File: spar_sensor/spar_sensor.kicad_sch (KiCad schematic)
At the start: 24 parts, among them J1 Conn_01x03_Pin, J2 Conn_01x04_Pin, J3 Conn_01x04_Pin, J4 AVR-ISP-6, Q1 MMS8550, Q2 2N7002K, SW1 SW_DPST_x2, U1 HX711, U2 ATtiny85-20M

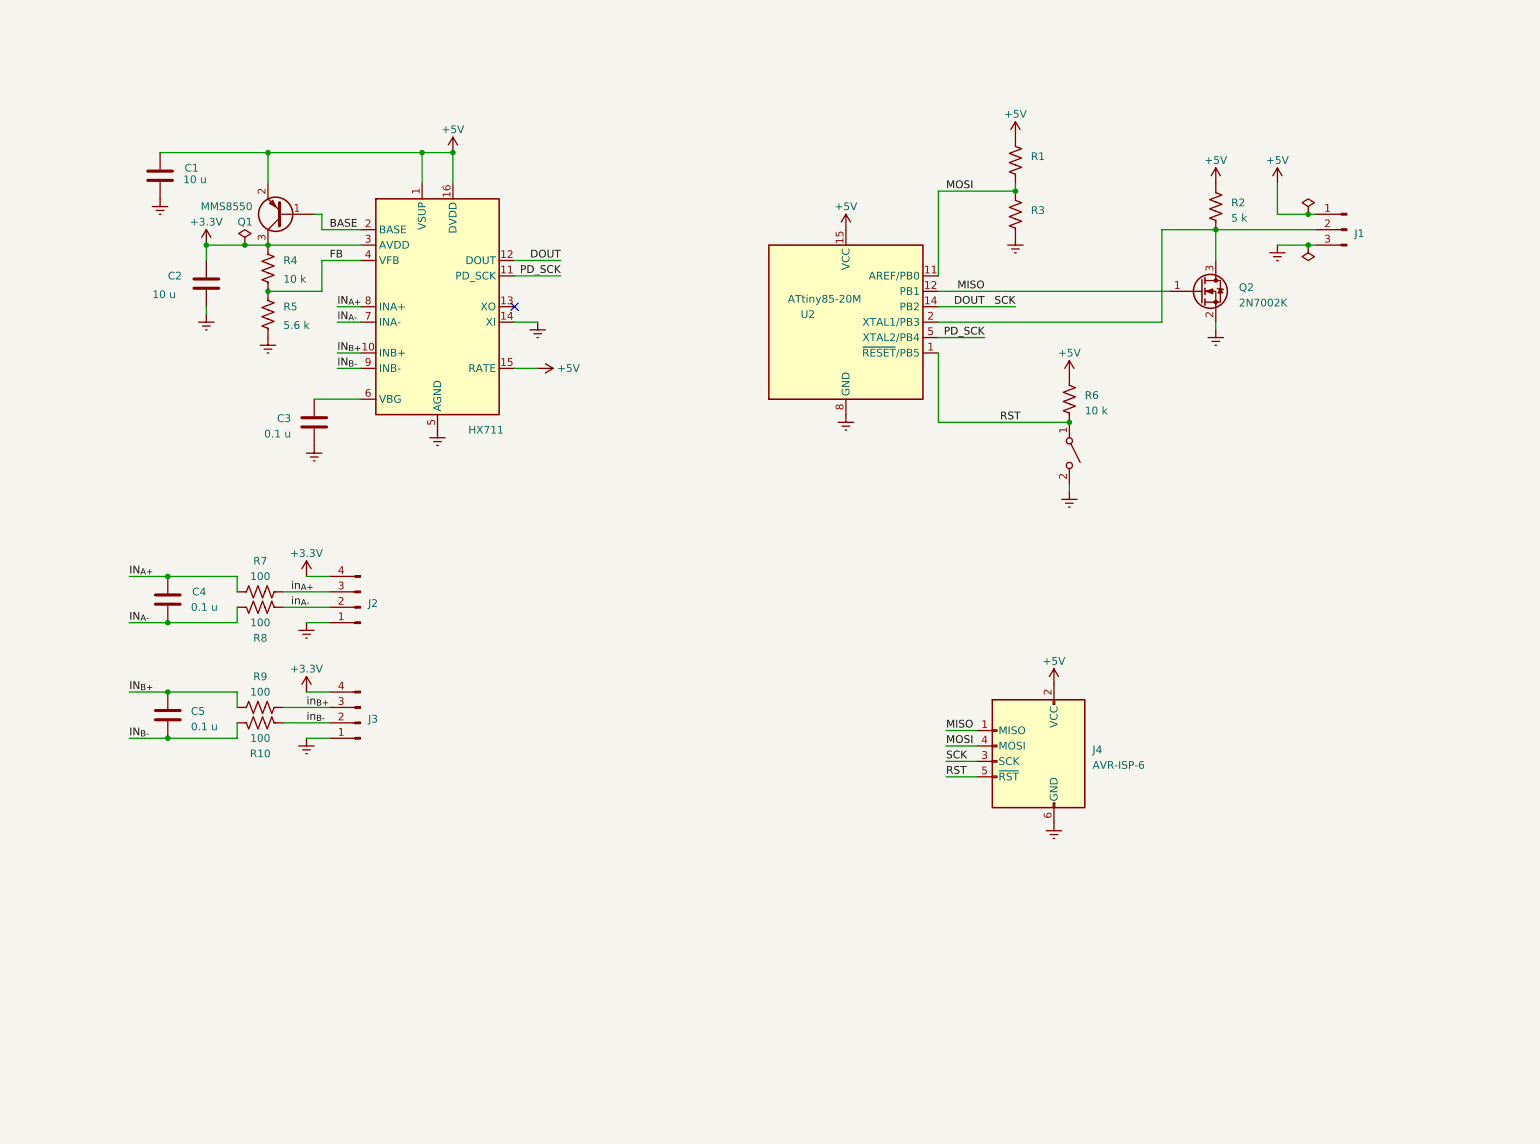
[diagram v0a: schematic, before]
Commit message: Touched up spar sensor to reflect parts as ordered
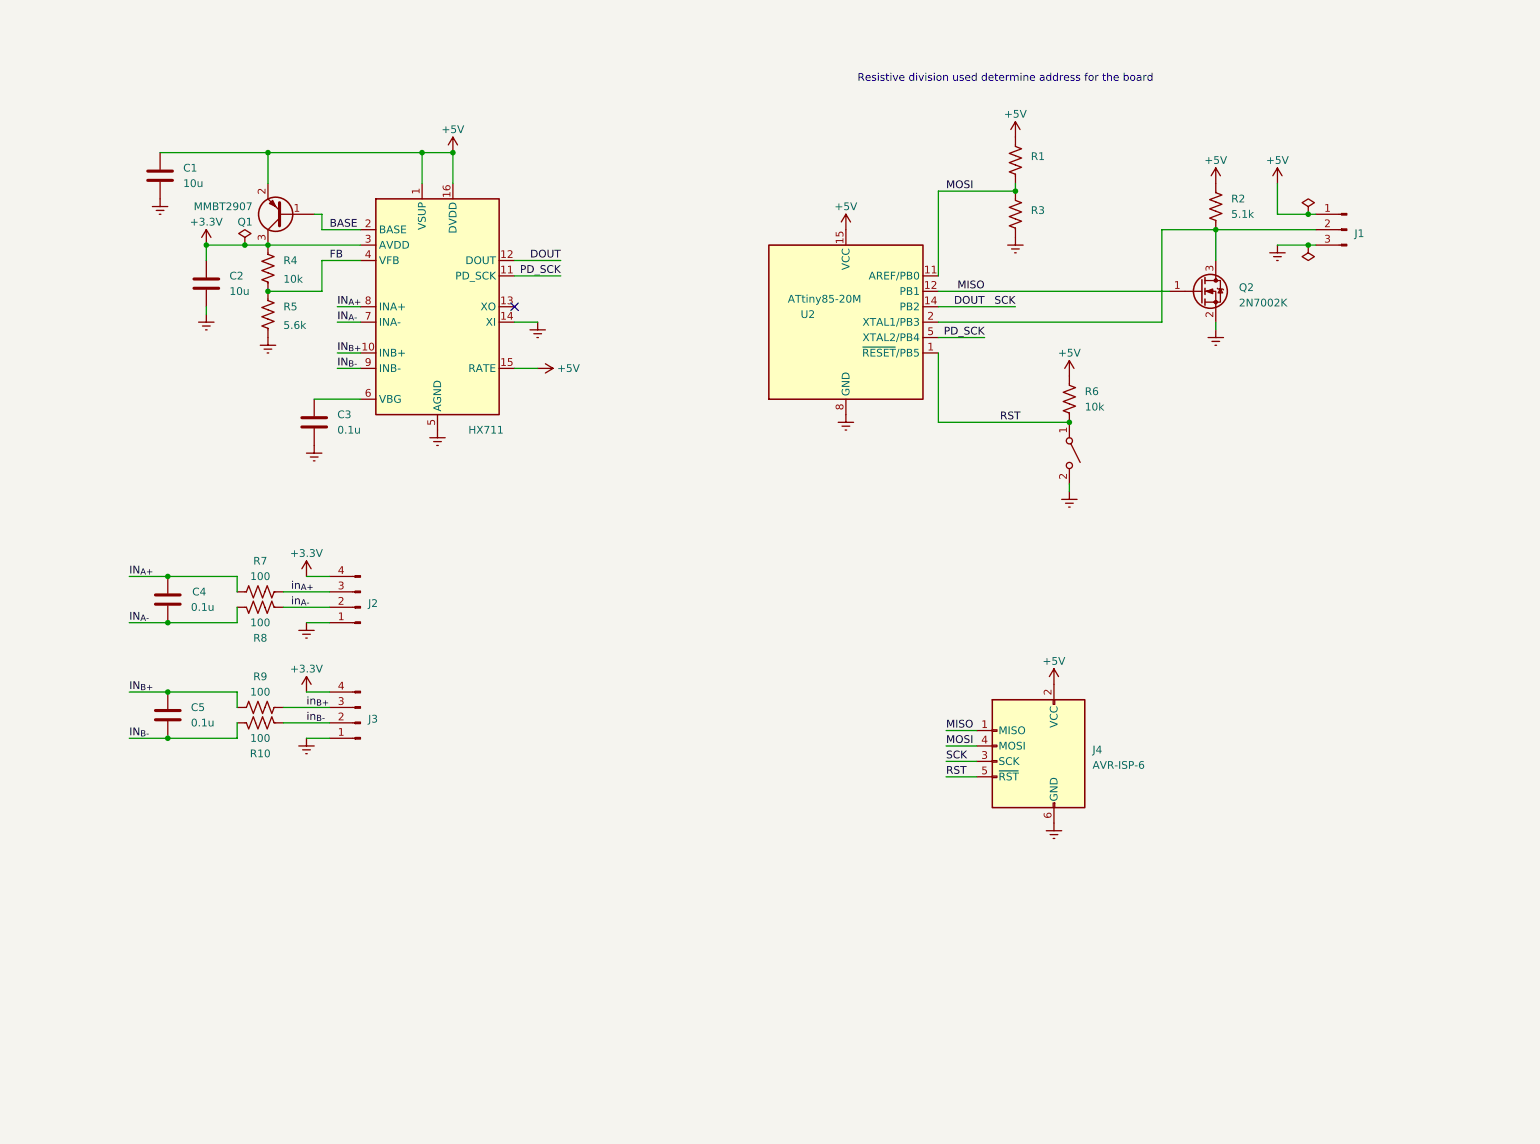
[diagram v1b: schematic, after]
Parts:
- C1, C2: value 10 u -> 10u
- C3, C4, C5: value 0.1 u -> 0.1u
- Q1: value MMS8550 -> MMBT2907
- R2: value 5 k -> 5.1k
- R4, R6: value 10 k -> 10k
- R5: value 5.6 k -> 5.6k
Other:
- note added: "Resistive division used determine address for the board"

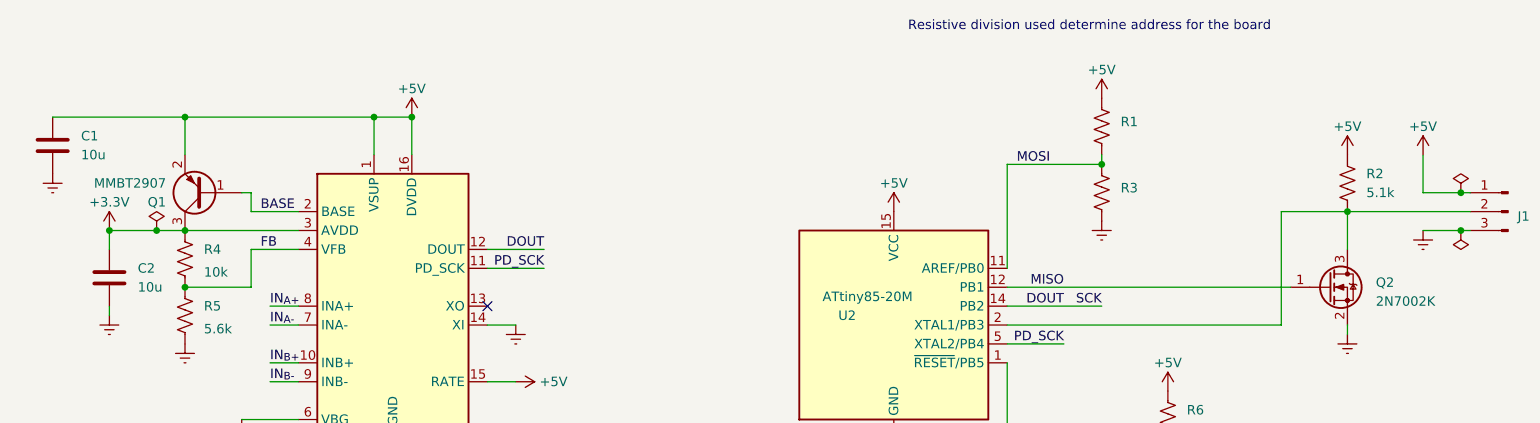
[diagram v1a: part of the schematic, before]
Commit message: Updated spar sensor to reflect order
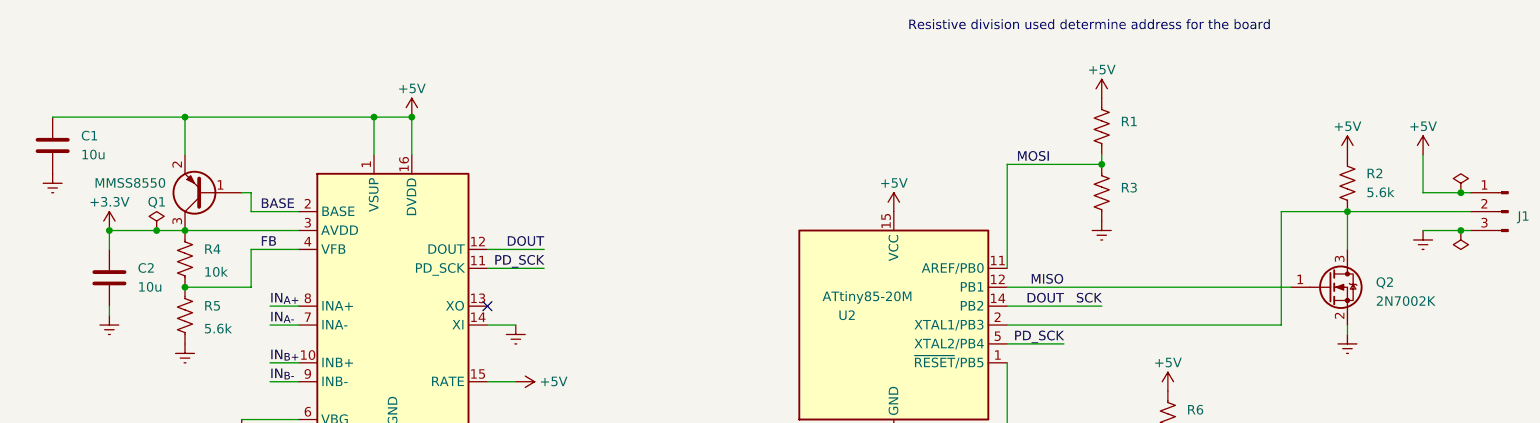
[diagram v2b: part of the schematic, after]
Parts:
- Q1: value MMBT2907 -> MMSS8550
- R2: value 5.1k -> 5.6k
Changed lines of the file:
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@@
       (effects (font (size 1.27 1.27)) (justify left))
     )
-    (property "Value" "5.1k" (at 223.52 46.99 0)
+    (property "Value" "5.6k" (at 223.52 46.99 0)
       (effects (font (size 1.27 1.27)) (justify left))
     )
@@
       (effects (font (size 1.27 1.27)) (justify left))
     )
-    (property "Value" "MMBT2907" (at 62.23 45.7201 0)
+    (property "Value" "MMSS8550" (at 62.23 45.7201 0)
       (effects (font (size 1.27 1.27)) (justify left))
     )
@@
       (effects (font (size 1.27 1.27)) hide)
     )
-    (property "Datasheet" "https://www.mouser.ca/datasheet/2/258/MMBT2907A_SOT_23_-2510709.pdf" (at 67.31 46.99 0)
-      (effects (font (size 1.27 1.27)) hide)
-    )
+    (property "Datasheet" "~" (at 67.31 46.99 0)
+      (effects (font (size 1.27 1.27)) hide)
+    )
